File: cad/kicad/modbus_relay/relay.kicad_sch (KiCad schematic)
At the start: 14 parts, among them Q2 BSS138

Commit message: Update of kicad and project files
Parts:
- removed C23: 100n, Capacitor_SMD:C_0805_2012Metric_Pad1.18x1.45mm_HandSolder, symbol Device:C
- removed D11, D12: BAS16, Diode_SMD:D_SOD-323_HandSoldering, symbol Device:D
- removed R23: 3k83, Resistor_SMD:R_0805_2012Metric_Pad1.20x1.40mm_HandSolder, symbol Device:R
- removed R24: 1k, Resistor_SMD:R_0805_2012Metric_Pad1.20x1.40mm_HandSolder, symbol Device:R
- removed R25: 100, Resistor_SMD:R_1206_3216Metric_Pad1.30x1.75mm_HandSolder, symbol Device:R
- added R28, R33: 332, Resistor_SMD:R_0805_2012Metric_Pad1.20x1.40mm_HandSolder, symbol Device:R
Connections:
- net +24V: no longer JP1.1 (A), K2.12
- net GND: now also JP1.1 (A), R28.2
- net RELAY_CTRL: now also JP1.2 (B), R33.1; no longer C22.1
- net VCC: now also K2.12
- net at K2.11: now also C22.1, R28.1, R33.2; no longer JP1.2 (B)
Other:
- moved on the sheet: JP1

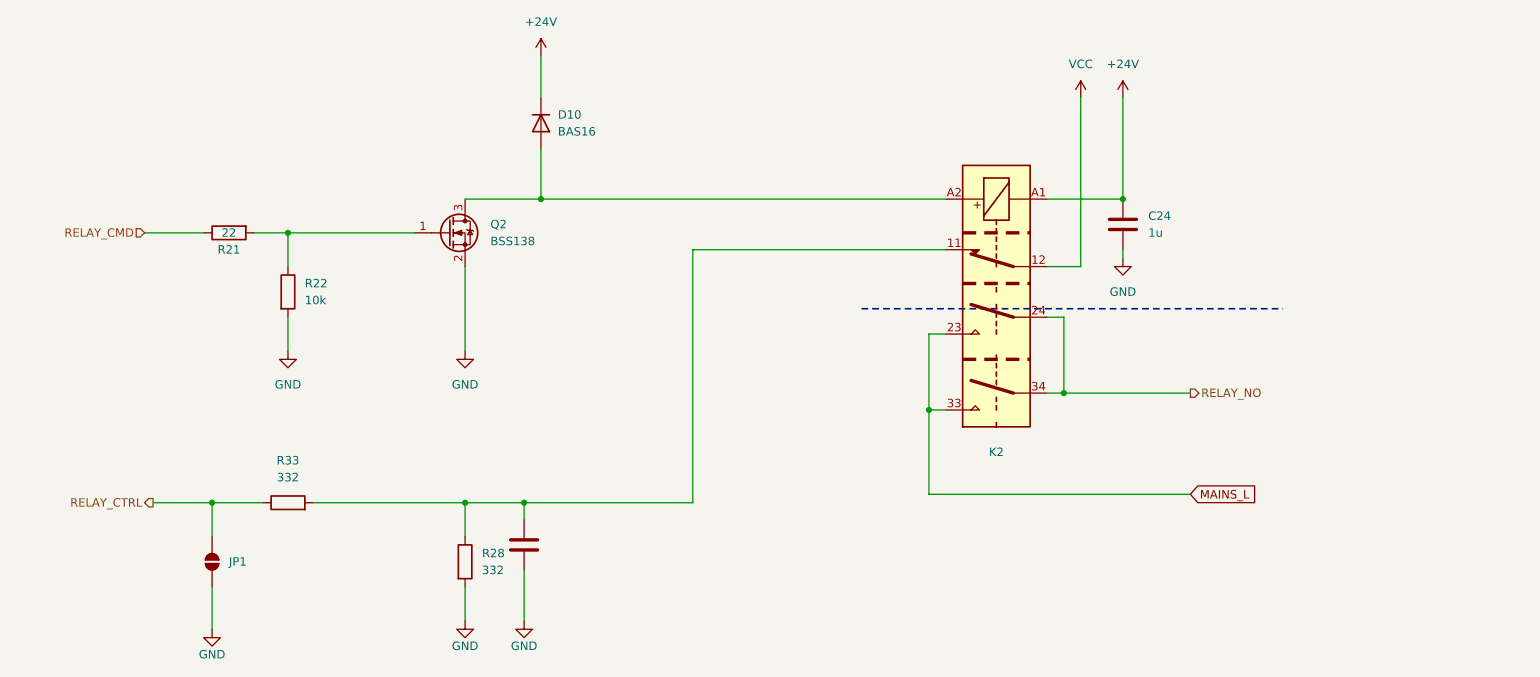
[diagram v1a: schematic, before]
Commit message: Double sided version
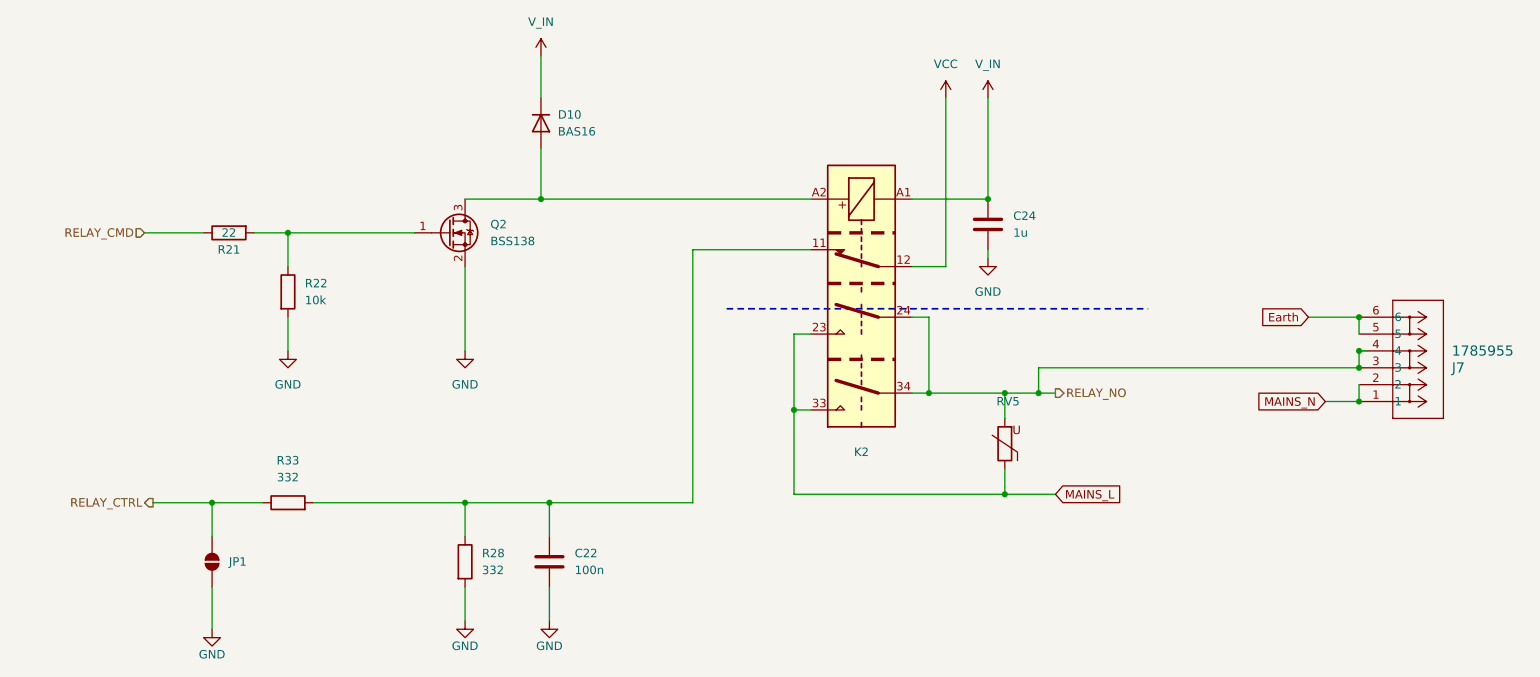
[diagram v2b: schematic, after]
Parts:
- added J7: 1785955, Phenix contact:CONN_1943548, symbol Phoeinx contact:1785955
- added RV5: 471K, adarwoo:MOV471, symbol Device:Varistor
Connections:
- net MAINS_L: now also RV5.1
- net RELAY_NO: now also J7.3, J7.4, RV5.2
- net +24V renamed V_IN
- new net Earth: J7.5, J7.6
- new net MAINS_N: J7.1, J7.2
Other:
- moved on the sheet: C24, K2

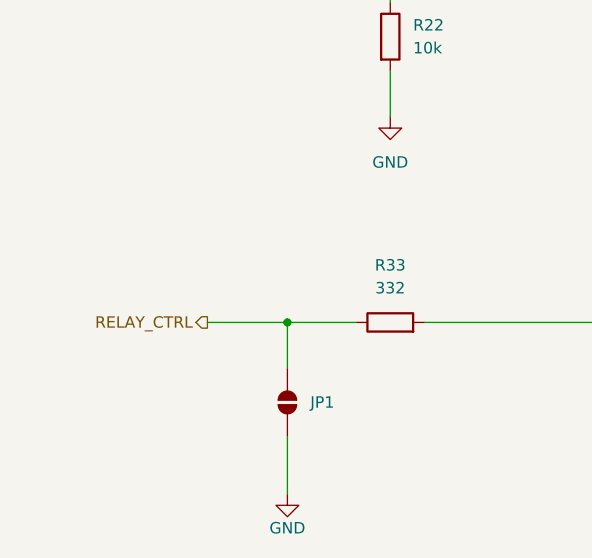
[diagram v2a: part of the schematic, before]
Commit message: New PCBs fixed and tested. Clean defs
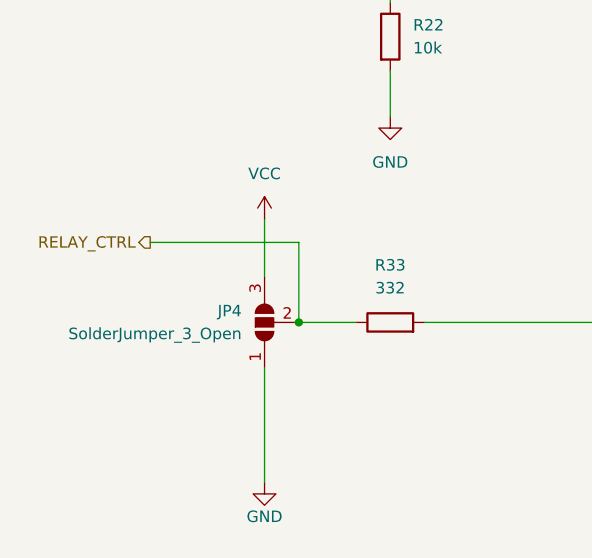
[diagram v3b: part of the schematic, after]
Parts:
- removed JP1: SolderJumper_2_Open, Jumper:SolderJumper-2_P1.3mm_Open_TrianglePad1.0x1.5mm, symbol Jumper:SolderJumper_2_Open
- added JP4: SolderJumper_3_Open, Jumper:SolderJumper-3_P1.3mm_Open_RoundedPad1.0x1.5mm_NumberLabels, symbol Jumper:SolderJumper_3_Open
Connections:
- net GND: now also JP4.1 (A)
- net RELAY_CTRL: now also JP4.2 (C)
- net VCC: now also JP4.3 (B)
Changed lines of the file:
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@@
+	)
+	(junction
+		(at 67.31 121.92)
+		(diameter 0)
+		(color 0 0 0 0)
 	)
 	(junction
@@
 	)
 	(junction
-		(at 66.04 121.92)
-		(diameter 0)
-		(color 0 0 0 0)
-	)
-	(junction
 		(at 190.5 105.41)
 		(diameter 0)
@@
 	(wire
 		(pts
+			(xy 63.5 139.7) (xy 63.5 127)
+		)
+		(stroke
+			(width 0)
+			(type default)
+		)
+	)
+	(wire
+		(pts
 			(xy 115.57 54.61) (xy 115.57 60.96)
 		)
@@
 		(pts
 			(xy 173.99 105.41) (xy 185.42 105.41)
-		)
-		(stroke
-			(width 0)
-			(type default)
-		)
-	)
-	(wire
-		(pts
-			(xy 66.04 134.62) (xy 66.04 140.97)
-		)
-		(stroke
-			(width 0)
-			(type default)
-		)
-	)
-	(wire
-		(pts
-			(xy 66.04 121.92) (xy 66.04 127)
 		)
 		(stroke
@@
 	(wire
 		(pts
+			(xy 63.5 110.49) (xy 63.5 116.84)
+		)
+		(stroke
+			(width 0)
+			(type default)
+		)
+	)
+	(wire
+		(pts
 			(xy 138.43 83.82) (xy 156.21 83.82)
 		)
@@
 	(wire
 		(pts
-			(xy 73.66 121.92) (xy 66.04 121.92)
+			(xy 67.31 113.03) (xy 67.31 121.92)
+		)
+		(stroke
+			(width 0)
+			(type default)
+		)
+	)
+	(wire
+		(pts
+			(xy 73.66 121.92) (xy 67.31 121.92)
 		)
 		(stroke
@@
 	(wire
 		(pts
-			(xy 66.04 121.92) (xy 57.15 121.92)
+			(xy 50.8 113.03) (xy 67.31 113.03)
 		)
 		(stroke
@@
 	(hierarchical_label "RELAY_CTRL"
 		(shape output)
-		(at 57.15 121.92 180)
+		(at 50.8 113.03 180)
 		(effects
 			(font
@@
 	)
 	(symbol
+		(lib_id "power:VCC")
+		(at 63.5 110.49 0)
+		(unit 1)
+		(exclude_from_sim no)
+		(in_bom yes)
+		(on_board yes)
+		(dnp no)
+		(fields_autoplaced yes)
+		(property "Reference" "#PWR01"
+			(at 63.5 114.3 0)
+			(effects
+				(font
+					(size 1.27 1.27)
+				)
+				(hide yes)
+			)
+		)
+		(property "Value" "VCC"
+			(at 63.5 105.41 0)
+			(effects
+				(font
+					(size 1.27 1.27)
+				)
+			)
+		)
+		(property "Footprint" ""
+			(at 63.5 110.49 0)
+			(effects
+				(font
+					(size 1.27 1.27)
+				)
+				(hide yes)
+			)
+		)
+		(property "Datasheet" ""
+			(at 63.5 110.49 0)
+			(effects
+				(font
+					(size 1.27 1.27)
+				)
+				(hide yes)
+			)
+		)
+		(property "Description" "Power symbol creates a global label with name \"VCC\""
+			(at 63.5 110.49 0)
+			(effects
+				(font
+					(size 1.27 1.27)
+				)
+				(hide yes)
+			)
+		)
+		(pin "1"
+		)
+		(instances
+			(project "modbus_relay"
+				(path "/aeb2e146-8395-44c2-9b78-4c462bf5527a/18dbe7c1-2b15-431b-88f0-18e45841562f"
+					(reference "#PWR052")
+					(unit 1)
+				)
+				(path "/aeb2e146-8395-44c2-9b78-4c462bf5527a/7021cce7-7815-417e-b7bd-c901451c1f81"
+					(reference "#PWR044")
+					(unit 1)
+				)
+				(path "/aeb2e146-8395-44c2-9b78-4c462bf5527a/9e1c4149-b70d-4529-8150-93d7ed1d7b16"
+					(reference "#PWR01")
+					(unit 1)
+				)
+			)
+		)
+	)
+	(symbol
 		(lib_id "Device:R")
 		(at 104.14 130.81 0)
@@
 	)
 	(symbol
-		(lib_id "Jumper:SolderJumper_2_Open")
-		(at 66.04 130.81 90)
+		(lib_id "Jumper:SolderJumper_3_Open")
+		(at 63.5 121.92 90)
 		(unit 1)
 		(exclude_from_sim no)
-		(in_bom yes)
+		(in_bom no)
 		(on_board yes)
 		(dnp no)
 		(fields_autoplaced yes)
-		(property "Reference" "JP1"
-			(at 68.58 130.8099 90)
-			(effects
-				(font
-					(size 1.27 1.27)
-				)
-				(justify right)
-			)
-		)
-		(property "Value" "SolderJumper_2_Open"
-			(at 62.23 130.81 0)
-			(effects
-				(font
-					(size 1.27 1.27)
-				)
-				(hide yes)
-			)
-		)
-		(property "Footprint" "Jumper:SolderJumper-2_P1.3mm_Open_TrianglePad1.0x1.5mm"
-			(at 66.04 130.81 0)
+		(property "Reference" "JP4"
+			(at 60.96 120.6499 90)
+			(effects
+				(font
+					(size 1.27 1.27)
+				)
+				(justify left)
+			)
+		)
+		(property "Value" "SolderJumper_3_Open"
+			(at 60.96 123.1899 90)
+			(effects
+				(font
+					(size 1.27 1.27)
+				)
+				(justify left)
+			)
+		)
+		(property "Footprint" "Jumper:SolderJumper-3_P1.3mm_Open_RoundedPad1.0x1.5mm_NumberLabels"
+			(at 63.5 121.92 0)
 			(effects
 				(font
@@
 		)
 		(property "Datasheet" "~"
-			(at 66.04 130.81 0)
-			(effects
-				(font
-					(size 1.27 1.27)
-				)
-				(hide yes)
-			)
-		)
-		(property "Description" "Solder Jumper, 2-pole, open"
-			(at 66.04 130.81 0)
+			(at 63.5 121.92 0)
+			(effects
+				(font
+					(size 1.27 1.27)
+				)
+				(hide yes)
+			)
+		)
+		(property "Description" "Solder Jumper, 3-pole, open"
+			(at 63.5 121.92 0)
 			(effects
 				(font
@@
 		(pin "1"
 		)
+		(pin "3"
+		)
 		(instances
-			(project "modbus_relay"
+			(project ""
 				(path "/aeb2e146-8395-44c2-9b78-4c462bf5527a/18dbe7c1-2b15-431b-88f0-18e45841562f"
-					(reference "JP3")
+					(reference "JP6")
 					(unit 1)
 				)
 				(path "/aeb2e146-8395-44c2-9b78-4c462bf5527a/7021cce7-7815-417e-b7bd-c901451c1f81"
-					(reference "JP2")
+					(reference "JP5")
 					(unit 1)
 				)
 				(path "/aeb2e146-8395-44c2-9b78-4c462bf5527a/9e1c4149-b70d-4529-8150-93d7ed1d7b16"
-					(reference "JP1")
+					(reference "JP4")
 					(unit 1)
 				)
@@
 	(symbol
 		(lib_id "power:GND")
-		(at 66.04 140.97 0)
+		(at 63.5 139.7 0)
 		(unit 1)
 		(exclude_from_sim no)
@@
 		(dnp no)
 		(property "Reference" "#PWR036"
-			(at 66.04 147.32 0)
+			(at 63.5 146.05 0)
 			(effects
 				(font
@@
 		)
 		(property "Value" "GND"
-			(at 66.04 144.78 0)
+			(at 63.5 143.51 0)
 			(effects
 				(font
@@
 		)
 		(property "Footprint" ""
-			(at 66.04 140.97 0)
+			(at 63.5 139.7 0)
 			(effects
 				(font
@@
 		)
 		(property "Datasheet" ""
-			(at 66.04 140.97 0)
+			(at 63.5 139.7 0)
 			(effects
 				(font
@@
 		)
 		(property "Description" "Power symbol creates a global label with name \"GND\" , ground"
-			(at 66.04 140.97 0)
-			(effects
-				(font
+			(at 63.5 139.7 0)
+			(effects
+				(font

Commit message: Improved front plate
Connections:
- net V_IN renamed VIN
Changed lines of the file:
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@@
 			)
 		)
-		(property "Value" "V_IN"
-			(at 182.88 55.88 0)
-			(effects
-				(font
-					(size 1.27 1.27)
-				)
+		(property "Value" "VIN"
+			(at 185.42 59.6899 0)
+			(effects
+				(font
+					(size 1.27 1.27)
+				)
+				(justify left)
 			)
 		)
@@
 			)
 		)
-		(property "Value" "V_IN"
-			(at 115.57 49.53 0)
-			(effects
-				(font
-					(size 1.27 1.27)
-				)
-			)
-		)
+		(property "Value" "VIN"
+			(at 118.11 53.3399 0)
+			(effects
+				(font
+					(size 1.27 1.27)
+				)
+				(justify left)
+			)
+		)
